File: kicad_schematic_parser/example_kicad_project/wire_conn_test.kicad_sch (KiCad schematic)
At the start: 12 parts, among them J2 Conn_01x04, U3 NCP1117-3.3_SOT223

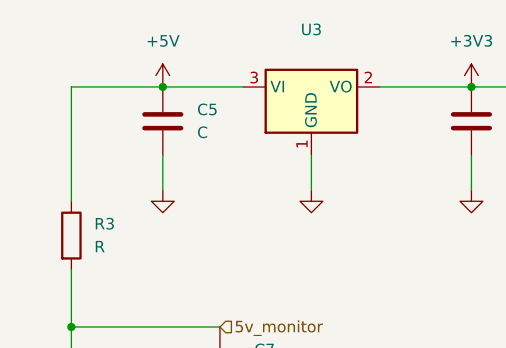
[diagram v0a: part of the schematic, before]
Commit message: sheets detecting component connections to pins
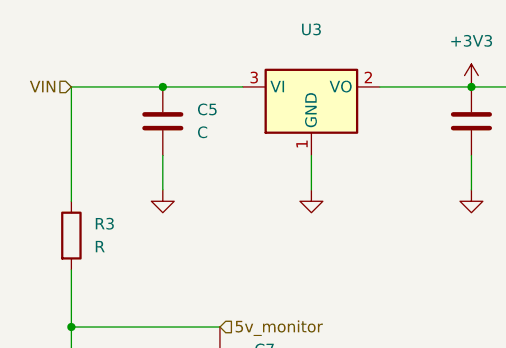
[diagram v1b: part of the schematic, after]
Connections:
- net +5V: no longer C5.1, R3.1, U3.3 (VI)
- new net VIN: C5.1, R3.1, U3.3 (VI)
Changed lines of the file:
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@@
+		)
+	)
+	(hierarchical_label "VIN"
+		(shape input)
+		(at 124.46 58.42 180)
+		(fields_autoplaced yes)
+		(effects
+			(font
+				(size 1.27 1.27)
+			)
+			(justify right)
 		)
 	)
@@
 					(unit 1)
 				)
-			)
-		)
-	)
-	(symbol
-		(lib_id "power:+5V")
-		(at 134.62 58.42 0)
-		(unit 1)
-		(exclude_from_sim no)
-		(in_bom yes)
-		(on_board yes)
-		(dnp no)
-		(fields_autoplaced yes)
-		(property "Reference" "#PWR03"
-			(at 134.62 62.23 0)
-			(effects
-				(font
-					(size 1.27 1.27)
-				)
-				(hide yes)
-			)
-		)
-		(property "Value" "+5V"
-			(at 134.62 53.34 0)
-			(effects
-				(font
-					(size 1.27 1.27)
-				)
-			)
-		)
-		(property "Footprint" ""
-			(at 134.62 58.42 0)
-			(effects
-				(font
-					(size 1.27 1.27)
-				)
-				(hide yes)
-			)
-		)
-		(property "Datasheet" ""
-			(at 134.62 58.42 0)
-			(effects
-				(font
-					(size 1.27 1.27)
-				)
-				(hide yes)
-			)
-		)
-		(property "Description" "Power symbol creates a global label with name \"+5V\""
-			(at 134.62 58.42 0)
-			(effects
-				(font
-					(size 1.27 1.27)
-				)
-				(hide yes)
-			)
-		)
-		(pin "1"
-		)
-		(instances
-			(project "example_kicad_project"
-				(path "/139408cf-b4ac-4ccf-8751-afbb6def1f13/8234fcde-2a25-40ed-bf1a-aa4bf9bd93ad"
-					(reference "#PWR03")
-					(unit 1)
-				)
